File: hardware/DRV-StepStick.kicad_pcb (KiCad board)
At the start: 4 copper layers, 36.7 x 39.4 mm, 23 parts, among them J1 PCIe_Stepper, J2 Conn_01x04_Male, J3 StepStickL, J4 StepStickR, J5 Conn_01x04, J6 Conn_02x04_Odd_Even, J7 Conn_01x02, J8 Screw_Terminal_01x02, U1 24LC02, U2 74LVC1G06

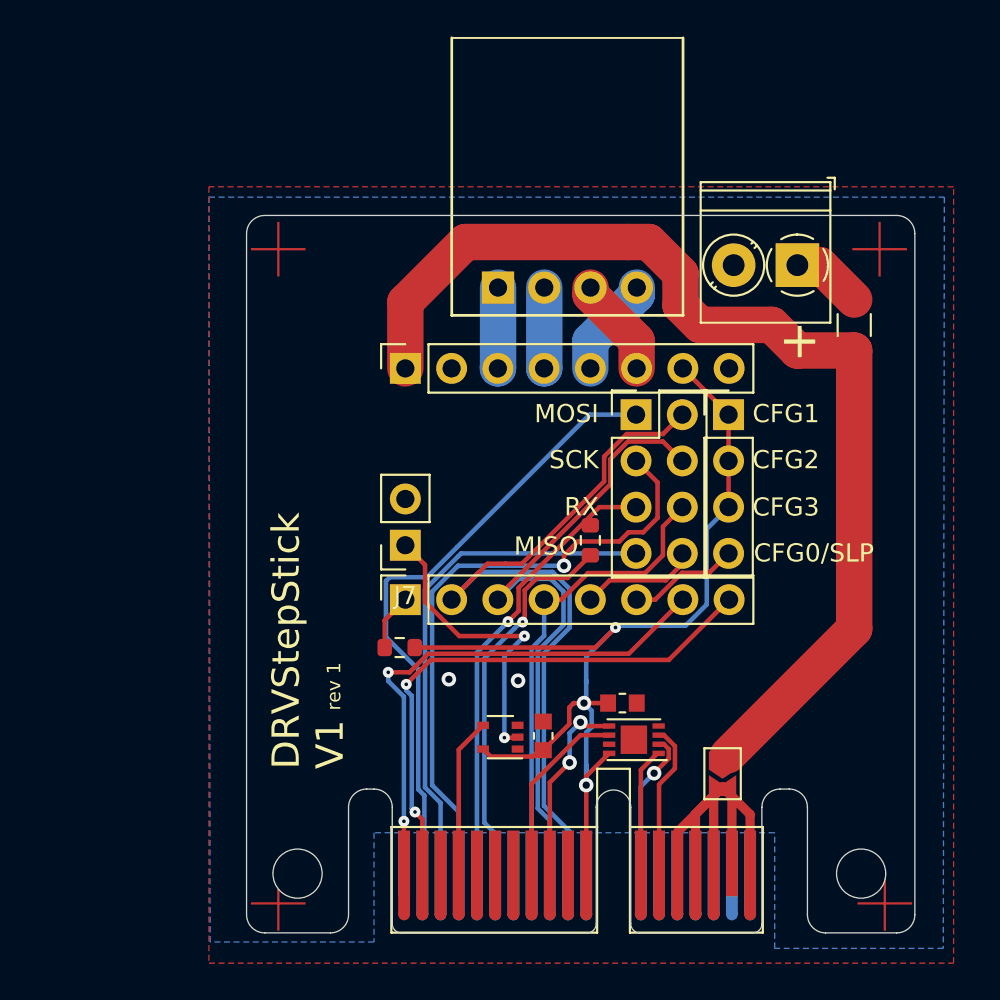
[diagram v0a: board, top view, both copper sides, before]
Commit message: Update the StepStick driver schematics, revert the routing.
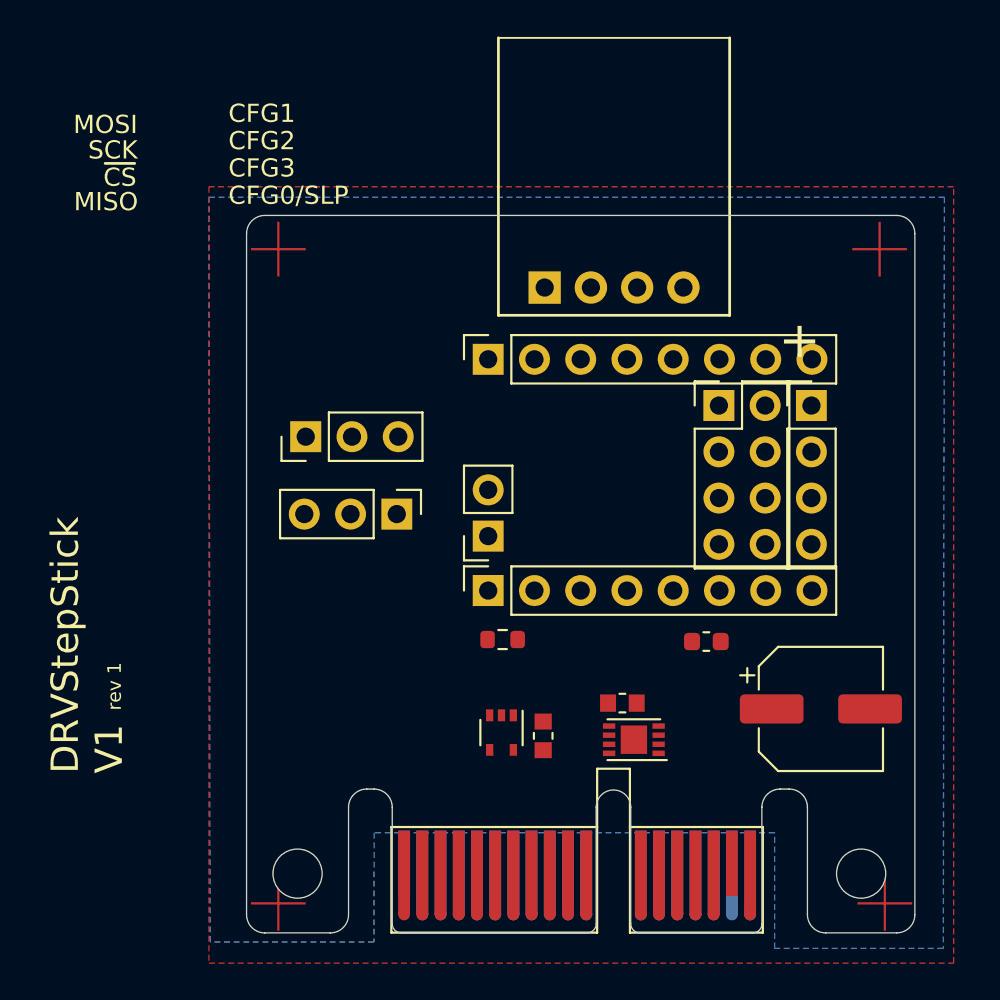
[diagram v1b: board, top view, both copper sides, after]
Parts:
- removed F1: 3A, Fuse:Fuse_1206_3216Metric
- removed J8: Screw_Terminal_01x02, TerminalBlock_Phoenix:TerminalBlock_Phoenix_PT-1,5-2-3.5-H_1x02_P3.50mm_Horizontal
- removed JP1: Use VM, Jumper:SolderJumper-2_P1.3mm_Open_TrianglePad1.0x1.5mm
- added C4: 100uF 35V, Capacitor_SMD:CP_Elec_6.3x7.7, F.Cu at (140.5, 101.7)
- added JP2: Serial, Connector_PinHeader_2.54mm:PinHeader_1x03_P2.54mm_Vertical, F.Cu at (117.2, 91.0)
- added JP3: Clock/Sleep, Connector_PinHeader_2.54mm:PinHeader_1x03_P2.54mm_Vertical, F.Cu at (112.2, 86.8)
- J2: value Conn_01x04_Male -> Motor
- J6: value Conn_02x04_Odd_Even -> SPI Mode
- moved LOGO1 14.4 mm to (156.1, 79.9)
- moved R2 8.46 mm to (134.2, 98.0), turned to 180 degrees
- moved R1 5.67 mm to (123.1, 97.9)
- moved J5 4.58 mm to (140.0, 85.0)
- moved J6 4.58 mm to (134.9, 85.0)
- moved J3 4.58 mm to (122.3, 95.2)
- moved J4 4.58 mm to (122.3, 82.5)
- moved J7 4.58 mm to (122.3, 92.2)
- moved J2 2.56 mm to (129.2, 78.6)
- moved U2 0.26 mm to (123.0, 103.0), turned to -90 degrees
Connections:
- net /CFG0 renamed /RST/MISO/UART
- J1 pad A1: (no net) -> /~CS
- J1 pad A10: /CFG1 -> (no net)
- J1 pad A5: /RX -> (no net)
- J1 pad A6: /TX -> /SERIAL
- J1 pad A7: (no net) -> /CLOCK
- J1 pad A8: /CFG3 -> (no net)
- J1 pad A9: /CFG2 -> (no net)
- J1 pad B14: /V_MOTORS -> /VBB
- J1 pad B15: /V_MOTORS -> /VBB
- J1 pad B16: /V_MOTORS -> /VBB
- J1 pad B17: /V_MOTORS -> /VBB
- J1 pad B18: /V_MOTORS -> /VBB
- J1 pad B3: (no net) -> /~ENABLE
- J1 pad B5: (no net) -> /~RESET
- J3 pad 1: /EN -> /~ENABLE
- J3 pad 2: /CFG1 -> /MS1/MOSI
- J3 pad 3: /CFG2 -> /MS2/SCK
- J3 pad 4: /CFG3 -> /MS3/~CS/UART
- J3 pad 6: /SLP -> /SLP/DCO/CLK/UART
- J5 pad 4: /SLP -> /~RESET
- J6 pad 2: /CFG1 -> /MS1/MOSI
- J6 pad 4: /CFG2 -> /MS2/SCK
- J6 pad 5: /RX -> /~CS
- J6 pad 6: /CFG3 -> /MS3/~CS/UART
- R1 pad 2: /EN -> /~ENABLE
- R2 pad 1: /TX -> /SLP/DCO/CLK/UART
- R2 pad 2: /RX -> VCC
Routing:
- net VCC: track 58.7 -> 0.00 mm, vias 3 -> 0
- net /VBB: track 58.2 -> 0.00 mm
- net /CFG1: track 42.2 -> 0.00 mm
- net /CFG2: track 35.8 -> 0.00 mm
- net /MOSI: track 34.4 -> 0.00 mm
- net /SCK: track 34.0 -> 0.00 mm, vias 1 -> 0
- net /DIR: track 30.4 -> 0.00 mm, vias 2 -> 0
- net /STEP: track 29.2 -> 0.00 mm, vias 2 -> 0
- net /MISO: track 28.3 -> 0.00 mm
- net /CFG3: track 26.1 -> 0.00 mm
- net /V_MOTORS: track 25.7 -> 0.00 mm
- net /RX: track 24.9 -> 0.00 mm, vias 1 -> 0
- net /TX: track 20.7 -> 0.00 mm, vias 1 -> 0
- net /DIAG: track 16.6 -> 0.00 mm, vias 2 -> 0
- net /SDA: track 10.6 -> 0.00 mm, vias 2 -> 0
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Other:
- board text added: "~CS"
- board text removed: "RX"

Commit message: Routed the StepStick adapter board 2 layers.
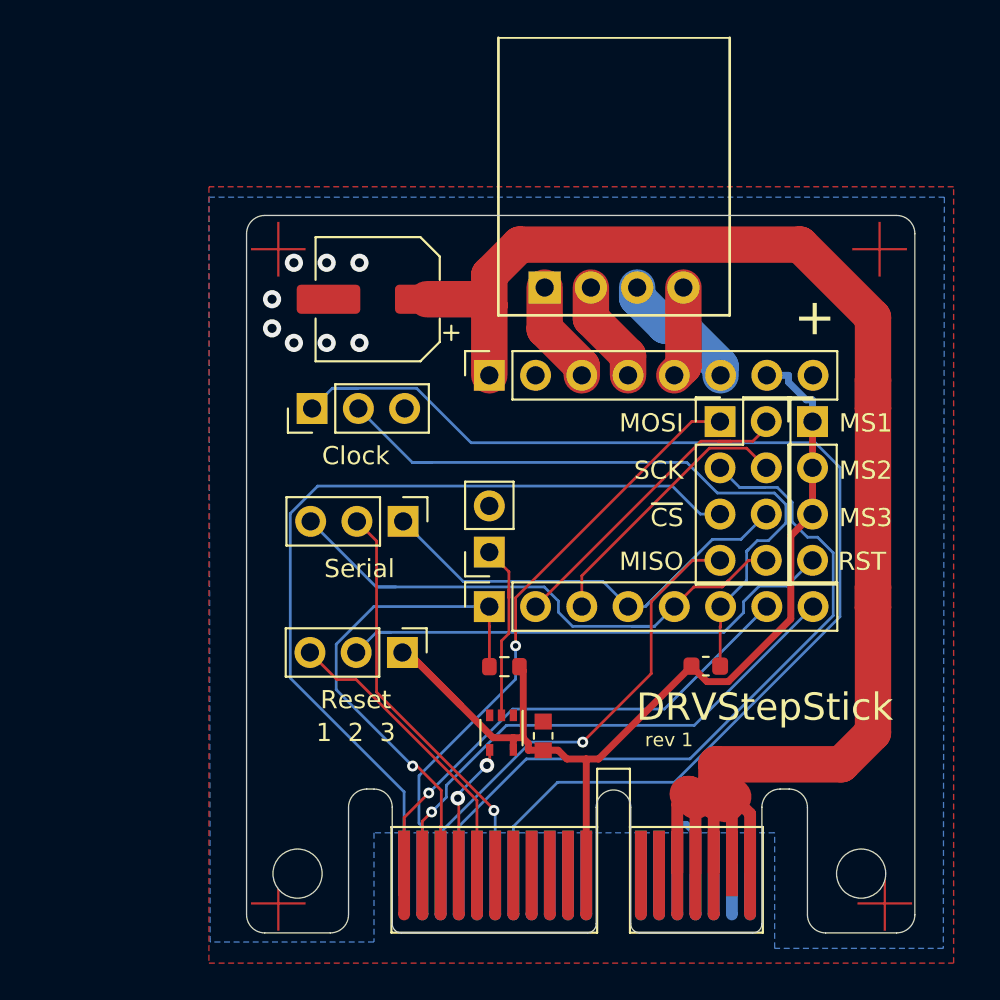
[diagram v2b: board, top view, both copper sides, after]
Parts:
- removed C1: 0.1uF, PrntrBoardV2:C_0603_1608Metric
- removed U1: 24LC02, PrntrBoardV2:TDFN-8-1EP_3x2mm_P0.5mm_EP1.56x1.45mm
- added JP4: Reset, Connector_PinHeader_2.54mm:PinHeader_1x03_P2.54mm_Vertical, F.Cu at (117.6, 98.6)
- moved C4 33.1 mm to (116.2, 79.2), turned to 180 degrees
- moved LOGO1 17.2 mm to (139.0, 77.8)
- moved JP3 1.59 mm to (112.6, 85.2)
- moved R1 1.49 mm to (123.2, 99.4)
- moved R2 1.35 mm to (134.2, 99.3)
- moved J7 0.88 mm to (122.3, 93.1)
- moved J3 0.88 mm to (122.3, 96.1)
- moved J4 0.88 mm to (122.3, 83.4)
- moved J5 0.88 mm to (140.1, 85.9)
- moved J6 0.88 mm to (135.0, 85.9)
- moved JP2 0.53 mm to (117.6, 91.4)
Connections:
- J1 pad A12: /ID_1 -> (no net)
- J1 pad B12: /ID_0 -> (no net)
- J1 pad B13: /ID_2 -> (no net)
- J1 pad B5: /~RESET -> /~ST_RESET
- J1 pad B8: /SCL -> (no net)
- J1 pad B9: /SDA -> (no net)
- J5 pad 4: /~RESET -> Net-(J5-Pad4)
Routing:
- net /VBB: track 0.00 -> 94.6 mm
- net /CLOCK: track 0.00 -> 66.1 mm
- net VCC: track 0.00 -> 58.6 mm
- net /~CS: track 0.00 -> 46.7 mm
- net /SCK: track 0.00 -> 41.5 mm
- net /SLP/DCO/CLK/UART: track 0.00 -> 37.6 mm
- net /MOSI: track 0.00 -> 32.6 mm, vias 0 -> 1
- net /RST/MISO/UART: track 0.00 -> 32.1 mm
- net /DIR: track 0.00 -> 29.5 mm, vias 0 -> 1
- net /MS3/~CS/UART: track 0.00 -> 28.9 mm
- net Net-(J5-Pad4): track 0.00 -> 28.3 mm
- net /STEP: track 0.00 -> 27.7 mm, vias 0 -> 1
- net /~ENABLE: track 0.00 -> 27.7 mm, vias 0 -> 1
- net /MISO: track 0.00 -> 26.1 mm, vias 0 -> 1
- net /SERIAL: track 0.00 -> 22.4 mm, vias 0 -> 1
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- removed copper zone on In1.Cu, net GND
- removed copper zone on In2.Cu, net GND
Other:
- copper layers 4 -> 2
- board text added: "1 2 3"
- board text added: "Clock"
- board text added: "DRVStepStick"
- board text added: "MS1"
- board text added: "MS2"
- board text added: "MS3"
- board text added: "RST"
- board text added: "Reset"
- board text added: "Serial"
- board text removed: "CFG0/SLP"
- board text removed: "CFG1"
- board text removed: "CFG2"
- board text removed: "CFG3"
- board text removed: "DRVStepStick V1"

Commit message: Small pcb corections
- populated GND vias around the pcb
- updated copyright info
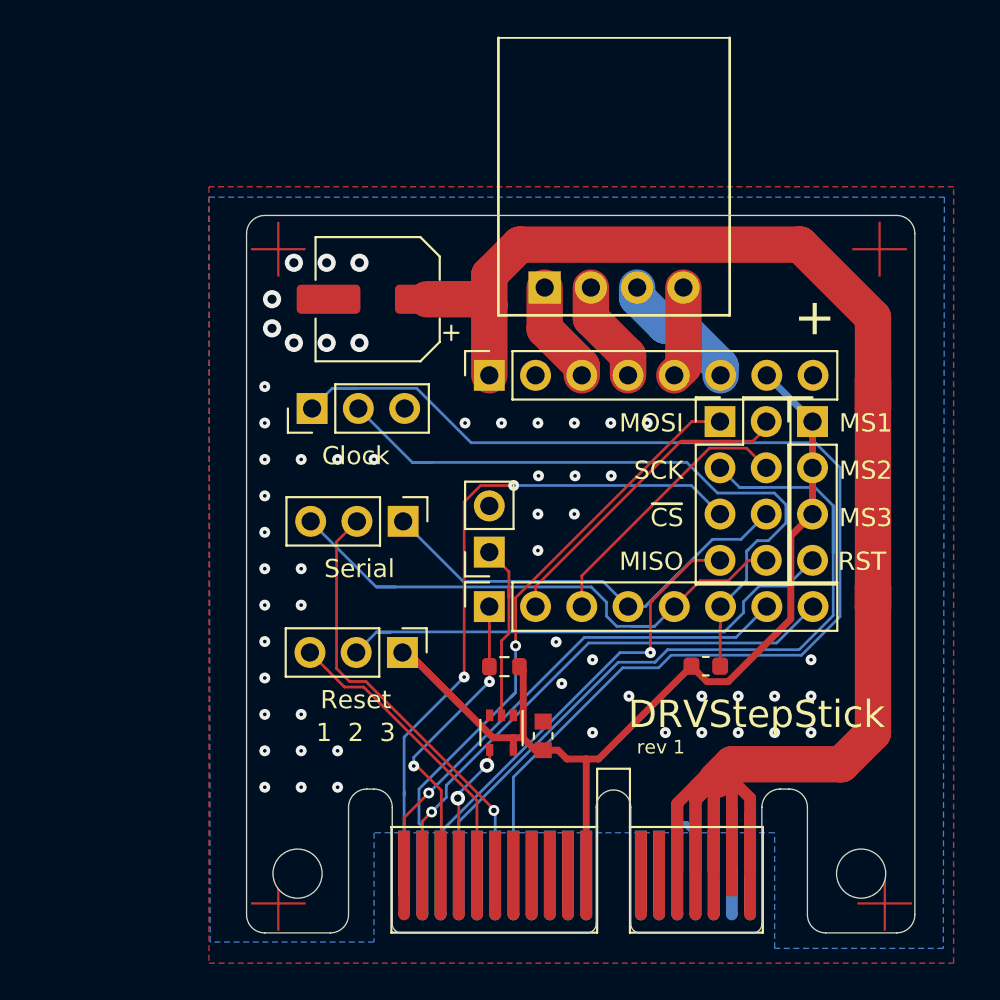
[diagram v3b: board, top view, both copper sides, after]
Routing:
- net /VBB: track 94.6 -> 116.9 mm
- net /~ENABLE: track 27.7 -> 17.1 mm, vias 1 -> 2
- net /~CS: track 46.7 -> 36.4 mm, vias 0 -> 2
- net /SCK: track 41.5 -> 45.1 mm
- net /MS1/MOSI: track 17.8 -> 19.5 mm
- net /CLOCK: track 66.1 -> 67.7 mm
- net /SERIAL: track 22.4 -> 23.9 mm
- net VCC: track 58.6 -> 57.5 mm
- net /MISO: track 26.1 -> 25.5 mm
- net GND: vias 8 -> 57
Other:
- board text added: "(c) Hijax_pl for iQury.us Jan 2021"
- board text removed: "(c) iQury.us Jan 2021"

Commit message: Update StepStick manufactirung files. Change copper zones with thermal relief. Added manufacturing scripts.
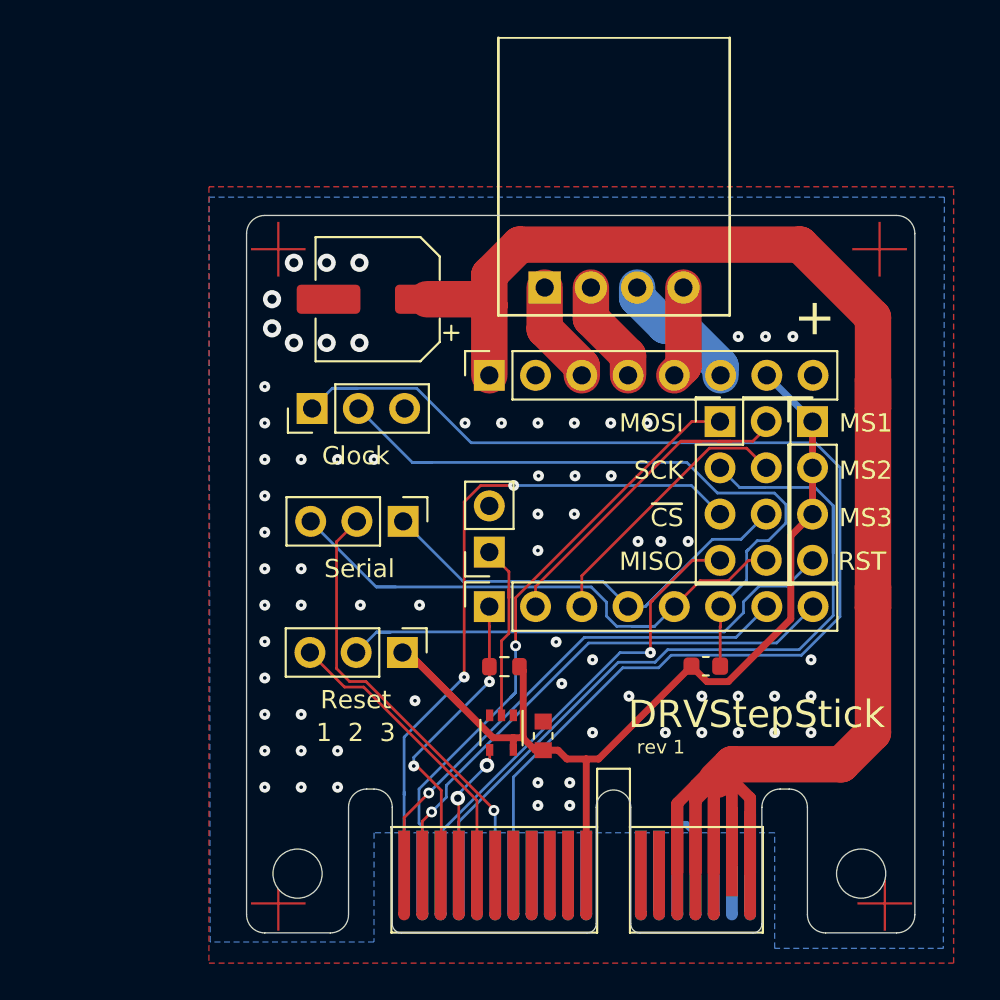
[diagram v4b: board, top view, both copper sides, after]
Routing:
- net GND: vias 57 -> 70
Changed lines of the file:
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@@
   (segment (start 117.653 106.413) (end 117.653 110.185) (width 0.1524) (layer "B.Cu") (net 1))
   (segment (start 123.67 89.43) (end 133.43 89.43) (width 0.1524) (layer "B.Cu") (net 1))
+  (via (at 115.25 96) (size 0.6) (drill 0.2) (layers "F.Cu" "B.Cu") (free) (net 2))
   (via (at 110 106) (size 0.6) (drill 0.2) (layers "F.Cu" "B.Cu") (free) (net 2))
   (via (at 110.4 79.2) (size 1) (drill 0.5) (layers "F.Cu" "B.Cu") (net 2))
+  (via (at 118.5 96) (size 0.6) (drill 0.2) (layers "F.Cu" "B.Cu") (free) (net 2))
+  (via (at 118.25 101.25) (size 0.6) (drill 0.2) (layers "F.Cu" "B.Cu") (free) (net 2))
   (via (at 112 96) (size 0.6) (drill 0.2) (layers "F.Cu" "B.Cu") (free) (net 2))
   (via (at 110 92) (size 0.6) (drill 0.2) (layers "F.Cu" "B.Cu") (free) (net 2))
   (via (at 138 101) (size 0.6) (drill 0.2) (layers "F.Cu" "B.Cu") (free) (net 2))
+  (via (at 137.5 81.25) (size 0.6) (drill 0.2) (layers "F.Cu" "B.Cu") (free) (net 2))
   (via (at 129.026443 88.90139) (size 0.6) (drill 0.2) (layers "F.Cu" "B.Cu") (free) (net 2))
   (via (at 112 106) (size 0.6) (drill 0.2) (layers "F.Cu" "B.Cu") (free) (net 2))
@@
   (via (at 110 90) (size 0.6) (drill 0.2) (layers "F.Cu" "B.Cu") (free) (net 2))
   (via (at 126 98.02151) (size 0.6) (drill 0.2) (layers "F.Cu" "B.Cu") (free) (net 2))
+  (via (at 125 105.75) (size 0.6) (drill 0.2) (layers "F.Cu" "B.Cu") (free) (net 2))
   (via (at 127 86) (size 0.6) (drill 0.2) (layers "F.Cu" "B.Cu") (free) (net 2))
   (via (at 138 103) (size 0.6) (drill 0.2) (layers "F.Cu" "B.Cu") (free) (net 2))
@@
   (via (at 126.308619 100.308619) (size 0.6) (drill 0.2) (layers "F.Cu" "B.Cu") (free) (net 2))
   (via (at 140 103) (size 0.6) (drill 0.2) (layers "F.Cu" "B.Cu") (free) (net 2))
+  (via (at 125 107) (size 0.6) (drill 0.2) (layers "F.Cu" "B.Cu") (free) (net 2))
   (via (at 110 86) (size 0.6) (drill 0.2) (layers "F.Cu" "B.Cu") (free) (net 2))
+  (via (at 133.25 92.5) (size 0.6) (drill 0.2) (layers "F.Cu" "B.Cu") (free) (net 2))
+  (via (at 126.75 107) (size 0.6) (drill 0.2) (layers "F.Cu" "B.Cu") (free) (net 2))
   (via (at 114 106) (size 0.6) (drill 0.2) (layers "F.Cu" "B.Cu") (free) (net 2))
   (via (at 110.4 80.8) (size 1) (drill 0.5) (layers "F.Cu" "B.Cu") (net 2))
+  (via (at 130.5 92.5) (size 0.6) (drill 0.2) (layers "F.Cu" "B.Cu") (free) (net 2))
   (via (at 110 104) (size 0.6) (drill 0.2) (layers "F.Cu" "B.Cu") (free) (net 2))
   (via (at 131 86) (size 0.6) (drill 0.2) (layers "F.Cu" "B.Cu") (free) (net 2))
@@
   (via (at 110 96) (size 0.6) (drill 0.2) (layers "F.Cu" "B.Cu") (free) (net 2))
   (via (at 115.2 77.2) (size 1) (drill 0.5) (layers "F.Cu" "B.Cu") (net 2))
+  (via (at 139 81.25) (size 0.6) (drill 0.2) (layers "F.Cu" "B.Cu") (free) (net 2))
   (via (at 136 101) (size 0.6) (drill 0.2) (layers "F.Cu" "B.Cu") (free) (net 2))
   (via (at 132 103) (size 0.6) (drill 0.2) (layers "F.Cu" "B.Cu") (free) (net 2))
@@
   (via (at 116 88) (size 0.6) (drill 0.2) (layers "F.Cu" "B.Cu") (free) (net 2))
   (via (at 127 91) (size 0.6) (drill 0.2) (layers "F.Cu" "B.Cu") (free) (net 2))
+  (via (at 126.75 105.75) (size 0.6) (drill 0.2) (layers "F.Cu" "B.Cu") (free) (net 2))
+  (via (at 136 81.25) (size 0.6) (drill 0.2) (layers "F.Cu" "B.Cu") (free) (net 2))
   (via (at 125.031901 88.90139) (size 0.6) (drill 0.2) (layers "F.Cu" "B.Cu") (free) (net 2))
   (via (at 128 99) (size 0.6) (drill 0.2) (layers "F.Cu" "B.Cu") (free) (net 2))
@@
   (via (at 114 104) (size 0.6) (drill 0.2) (layers "F.Cu" "B.Cu") (free) (net 2))
   (via (at 113.4 81.6) (size 1) (drill 0.5) (layers "F.Cu" "B.Cu") (net 2))
+  (via (at 131.75 92.5) (size 0.6) (drill 0.2) (layers "F.Cu" "B.Cu") (free) (net 2))
   (via (at 140 101) (size 0.6) (drill 0.2) (layers "F.Cu" "B.Cu") (free) (net 2))
   (segment (start 133.653 108.5406) (end 133.1542 108.0418) (width 0.381) (layer "B.Cu") (net 2))
@@
   (segment (start 116.1271 97.4929) (end 116.149791 97.470209) (width 0.1524) (layer "B.Cu") (net 25))
   (zone (net 2) (net_name "GND") (layer "F.Cu") (hatch edge 0.508)
-    (connect_pads yes (clearance 0.2032))
+    (connect_pads (clearance 0.2032))
     (min_thickness 0.254) (filled_areas_thickness no)
     (fill yes (thermal_gap 0.508) (thermal_bridge_width 0.508))
@@
   )
   (zone (net 2) (net_name "GND") (layer "B.Cu") (hatch edge 0.508)
-    (connect_pads yes (clearance 0.1524))
+    (connect_pads (clearance 0.1524))
     (min_thickness 0.254) (filled_areas_thickness no)
     (fill yes (thermal_gap 0.508) (thermal_bridge_width 0.508))
